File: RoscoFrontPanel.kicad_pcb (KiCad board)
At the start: 2 copper layers, 160 x 39 mm, 33 parts, among them J1 Conn_01x02_Male, J10 Conn_01x04_Male, J11 DB9_Male, J12 DB9_Male, J2 Conn_01x02_Male, J3 Conn_01x02_Male, J4 Conn_01x02_Male, J5 Conn_01x02_Male, J6 Conn_01x02_Male, J7 PJ-037B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

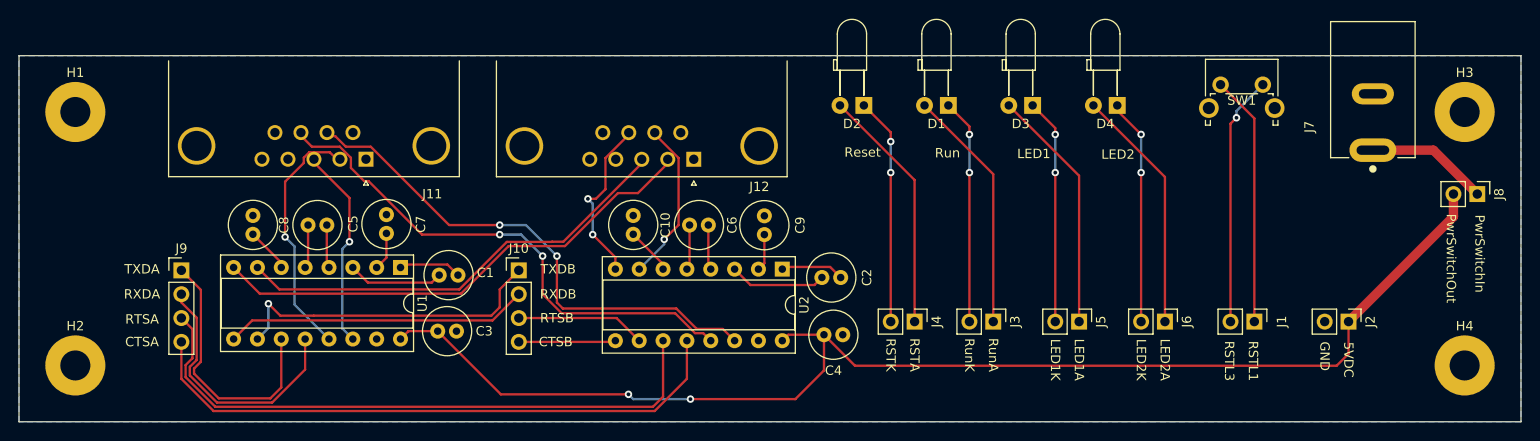
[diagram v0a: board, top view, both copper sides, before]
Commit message: Minor design fixups
* Added rounded corners
* Rerouted tracks too close too pad
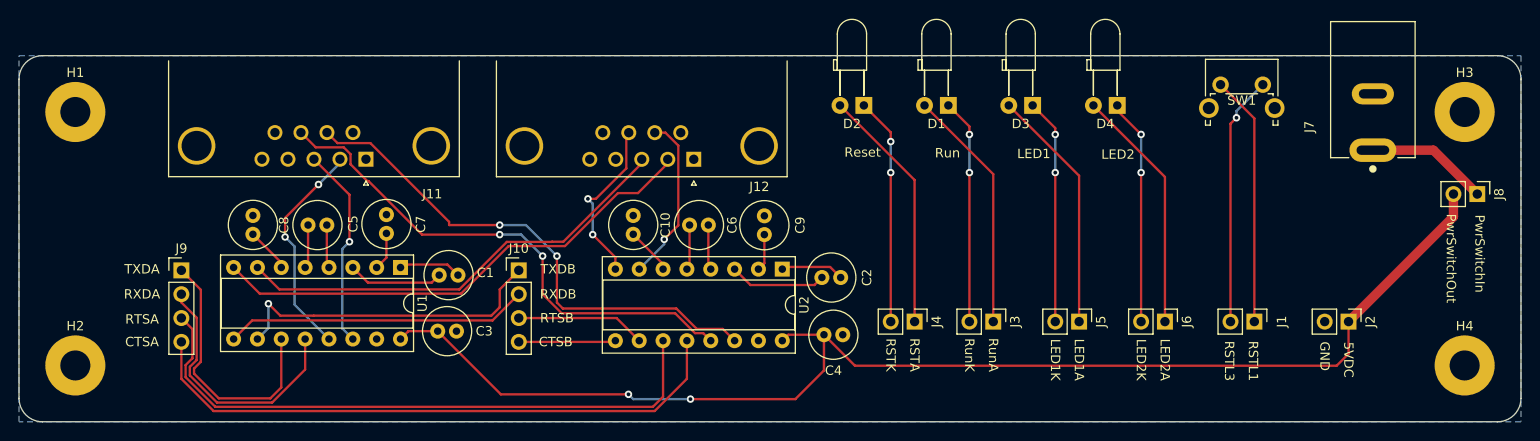
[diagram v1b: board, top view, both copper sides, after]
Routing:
- net /RS232/RXDAOUT: track 26.7 -> 23.5 mm, vias 1 -> 2
- net /RS232/RTSBOUT: track 17.0 -> 18.2 mm
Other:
- outline, holes or cut-outs redrawn
